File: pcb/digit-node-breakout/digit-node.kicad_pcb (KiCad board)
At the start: 2 copper layers, 53.3 x 30.5 mm, 20 parts, among them J1 Conn_01x09_Male, J2 STM32_SWD, Q1 PZT2222A, Q2 PZT2222A, U1 STM32F030F4Px

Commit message: Use a transistor array instead of two discrete transistors
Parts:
- removed Q2: PZT2222A, Package_TO_SOT_SMD:SOT-223-3_TabPin2
- Q1: value PZT2222A -> BC847BS; footprint Package_TO_SOT_SMD:SOT-223-3_TabPin2 -> Package_TO_SOT_SMD:SOT-363_SC-70-6
- moved Q1 7.62 mm to (137.2, 85.1), turned to 270 degrees
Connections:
- Q1 pad 1: Net-(Q1-Pad1) -> GND
- Q1 pad 3: GND -> Net-(Q1-Pad3)
- R1 pad 2: Net-(Q1-Pad2) -> Net-(Q1-Pad6)
- R2 pad 2: Net-(Q2-Pad2) -> Net-(Q1-Pad3)
- U1 pad 10: Net-(Q2-Pad1) -> Net-(Q1-Pad2)
- U1 pad 11: Net-(Q1-Pad1) -> Net-(Q1-Pad5)
- U1 pad 8: /led_matrix/led_45 -> /led_matrix/led_23
- U1 pad 9: /led_matrix/led_23 -> /led_matrix/led_45
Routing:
- net GND: track 7.04 -> 50.0 mm, vias 0 -> 1
- net Net-(Q1-Pad6): track 0.00 -> 12.0 mm
- net Net-(Q2-Pad2): track 10.0 -> 0.00 mm
- net Net-(Q1-Pad5): track 0.00 -> 9.25 mm
- net Net-(Q1-Pad1): track 9.19 -> 0.00 mm
- net Net-(Q1-Pad3): track 0.00 -> 8.72 mm
- net Net-(Q2-Pad1): track 3.56 -> 0.00 mm
- net /led_matrix/led_23: track 63.9 -> 62.2 mm
- net /led_matrix/led_89: track 35.4 -> 33.9 mm
- net /led_matrix/led_67: track 40.1 -> 41.3 mm
- net /led_matrix/led_01: track 60.3 -> 59.6 mm
- net VDD: track 54.7 -> 55.5 mm
- net /led_matrix/led_45: track 43.6 -> 44.2 mm
- net Net-(J1-Pad4): track 26.7 -> 26.1 mm

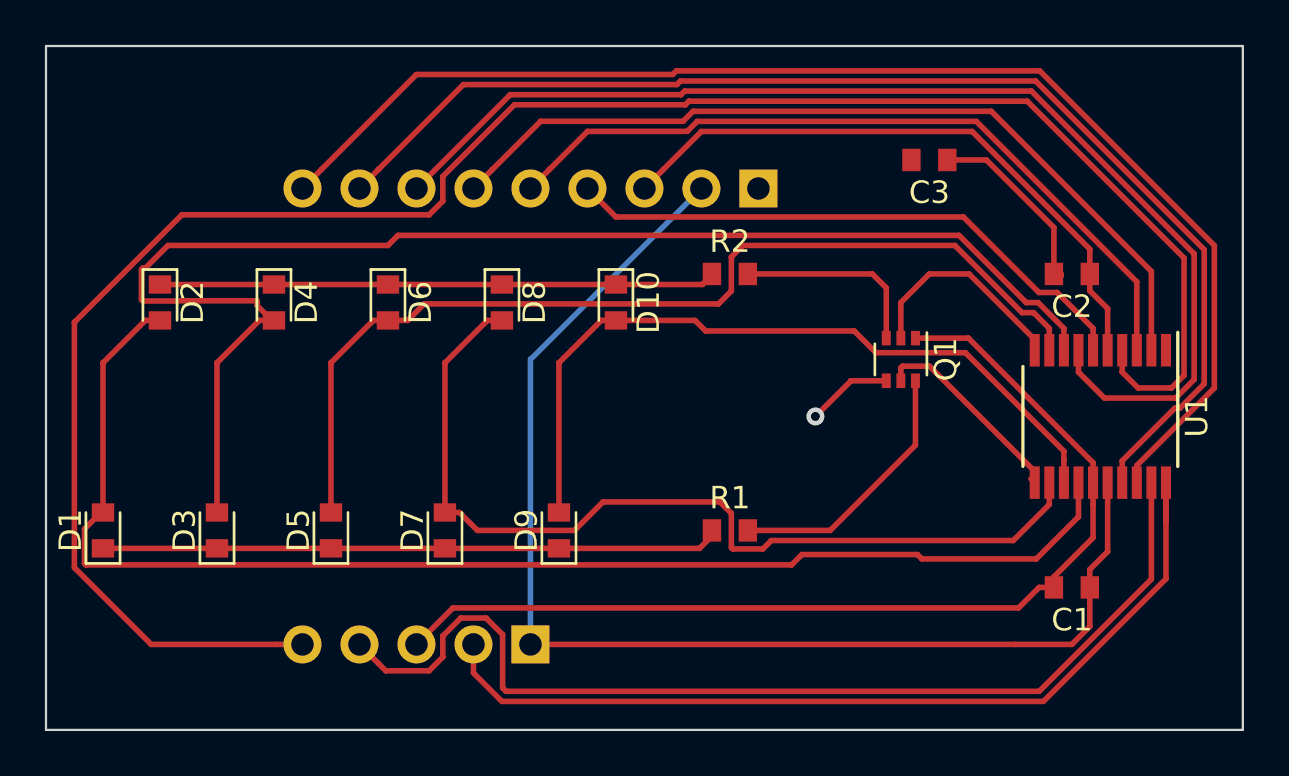
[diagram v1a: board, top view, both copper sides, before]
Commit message: Adapted PCB for Mentorspace mill design rules
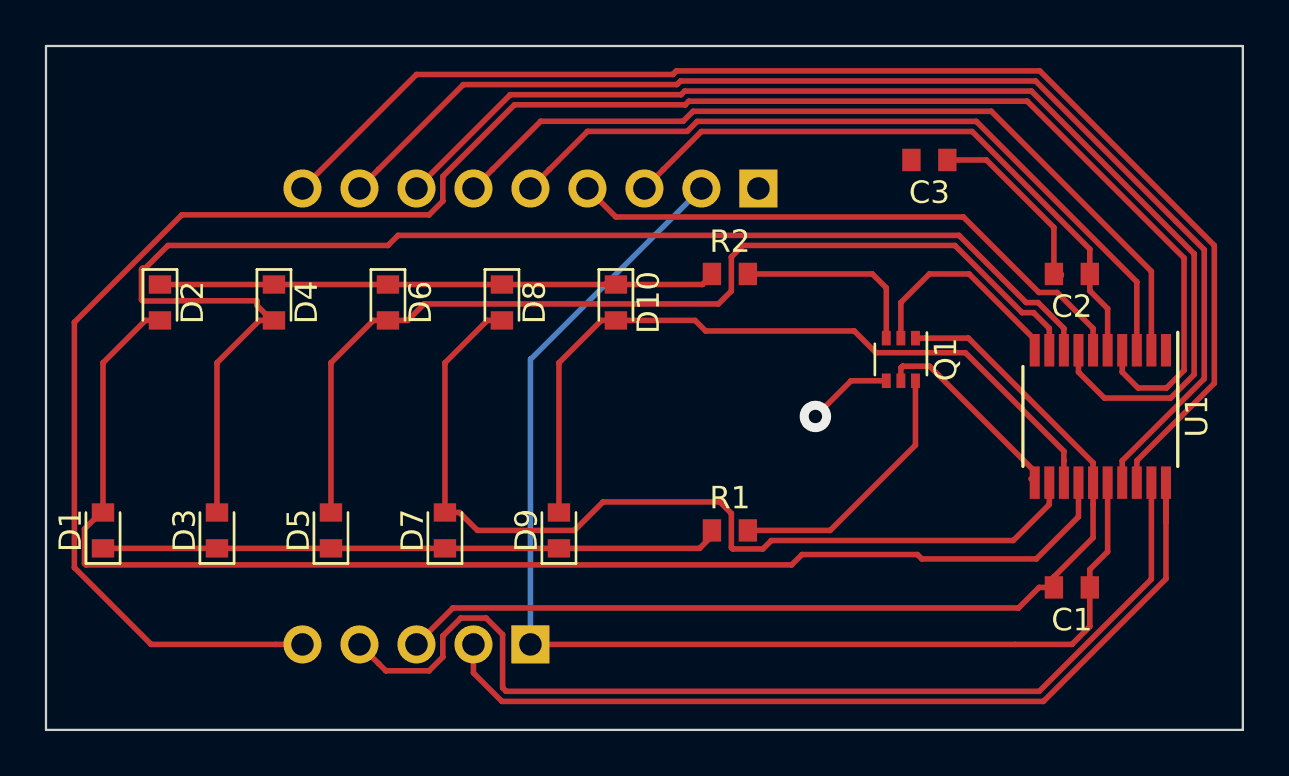
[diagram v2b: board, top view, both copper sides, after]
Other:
- net class Default: via_dia 0.8 -> 1.4; via_drill 0.4 -> 0.6
